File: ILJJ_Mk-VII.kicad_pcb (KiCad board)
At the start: 2 copper layers, 48.3 x 99.1 mm, 29 parts, among them J1 Conn_02x12, U1 74LS00, U10 74LS00, U11 74LS00, U2 74LS00, U3 74LS00, U4 74LS00, U5 74LS00, U6 74LS00, U7 74LS00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

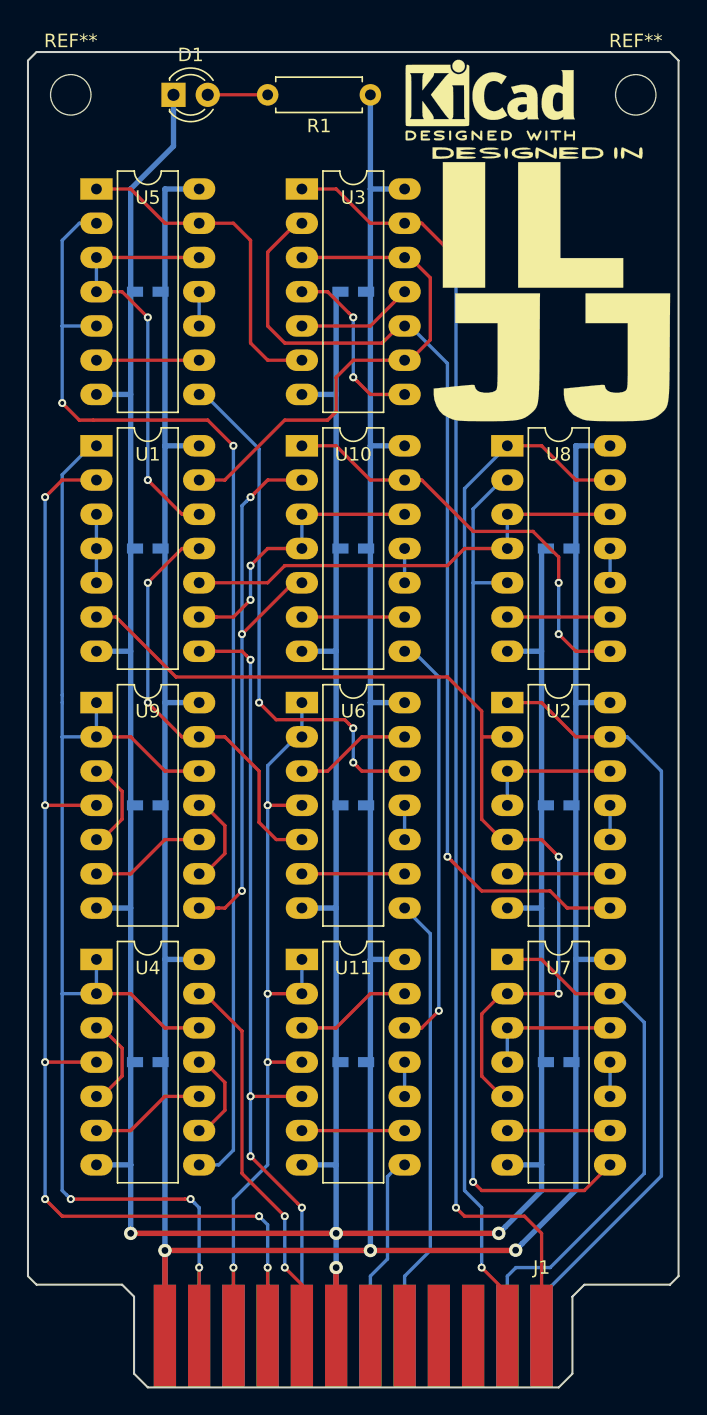
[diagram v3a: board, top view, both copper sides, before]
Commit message: [fix] ICの干渉を解消 / ILJJのロゴを小さく
かなりレイアウトが変わった
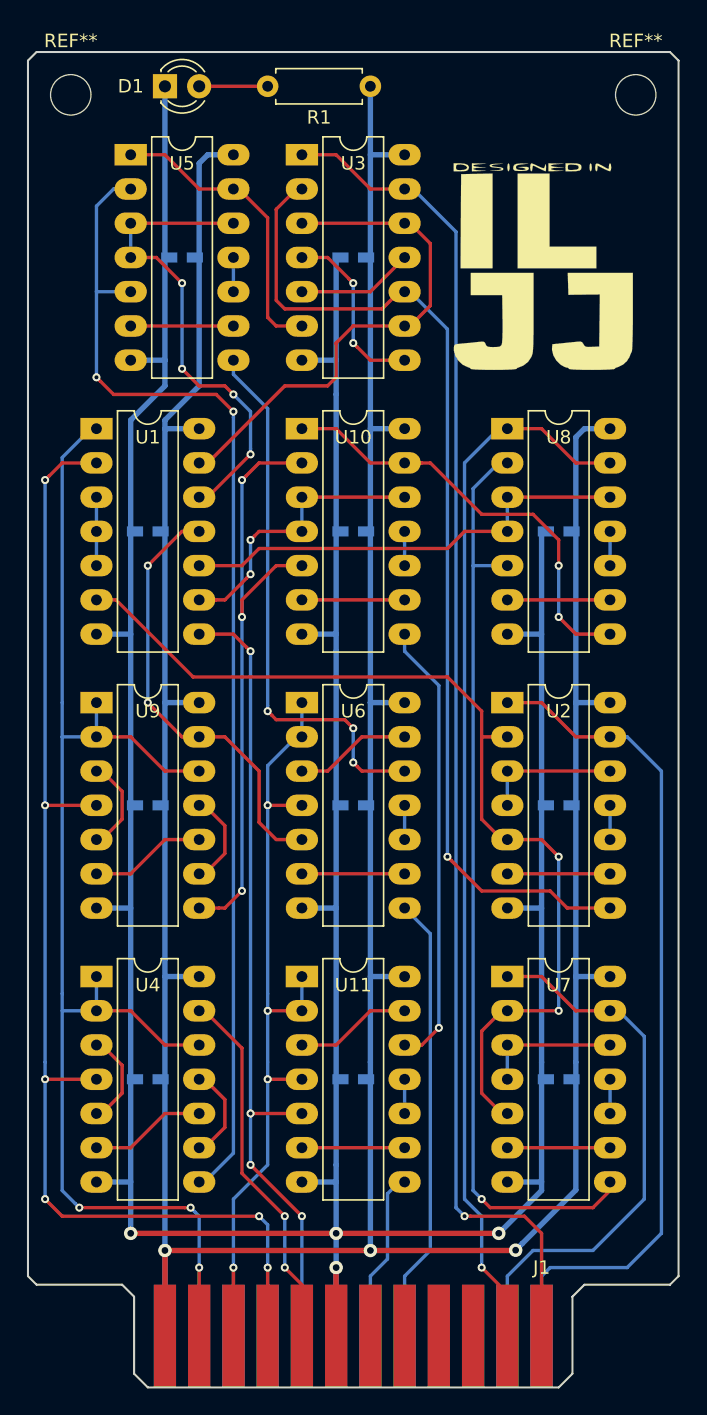
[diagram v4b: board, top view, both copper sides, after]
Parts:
- removed the G*** at (140.3, 67.9)
- removed REF***: KiCad-Logo2_6mm_SilkScreen, Symbols:KiCad-Logo2_6mm_SilkScreen
- added G***: LOGO, fplib:designed-in-ILJJ-small, F.Cu at (139.7, 66.7)
- moved C1 3.59 mm to (113.0, 66.0)
- moved U5 3.59 mm to (109.2, 58.4)
- moved U3 2.54 mm to (121.9, 58.4)
- moved C5 2.54 mm to (125.7, 66.0)
- moved U1 1.27 mm to (106.7, 78.7)
- moved U10 1.27 mm to (121.9, 78.7)
- moved U8 1.27 mm to (137.2, 78.7)
- moved C11 1.27 mm to (141.0, 127.0)
- moved C2 1.27 mm to (110.5, 86.4)
- moved C4 1.27 mm to (110.5, 127.0)
- moved C6 1.27 mm to (125.7, 86.4)
- moved C8 1.27 mm to (125.7, 127.0)
- moved C9 1.27 mm to (141.0, 86.4)
- moved U11 1.27 mm to (121.9, 119.4)
- moved U4 1.27 mm to (106.7, 119.4)
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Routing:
- net VCC: track 296.2 -> 300.9 mm
- net GND: track 278.6 -> 282.7 mm
- net Net-(U1-Pad12): track 31.7 -> 35.8 mm, vias 2 -> 4
- net /B0: track 59.1 -> 62.5 mm
- net Net-(U3-Pad6): track 25.0 -> 22.3 mm
- net /FA1_B: track 67.1 -> 69.8 mm
- net /FA1_Cin: track 43.5 -> 45.9 mm
- net /FA1_S: track 31.2 -> 33.3 mm
- net /A0: track 98.8 -> 100.9 mm, vias 2 -> 1
- net /FA0_B: track 74.7 -> 76.7 mm
- net /SUB_FLAG: track 72.3 -> 74.1 mm
- net /Cin: track 29.2 -> 27.5 mm
- net /FA0_S: track 39.3 -> 41.0 mm
- net /A1: track 77.3 -> 79.0 mm
- net Net-(U10-Pad1): track 32.5 -> 33.8 mm
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
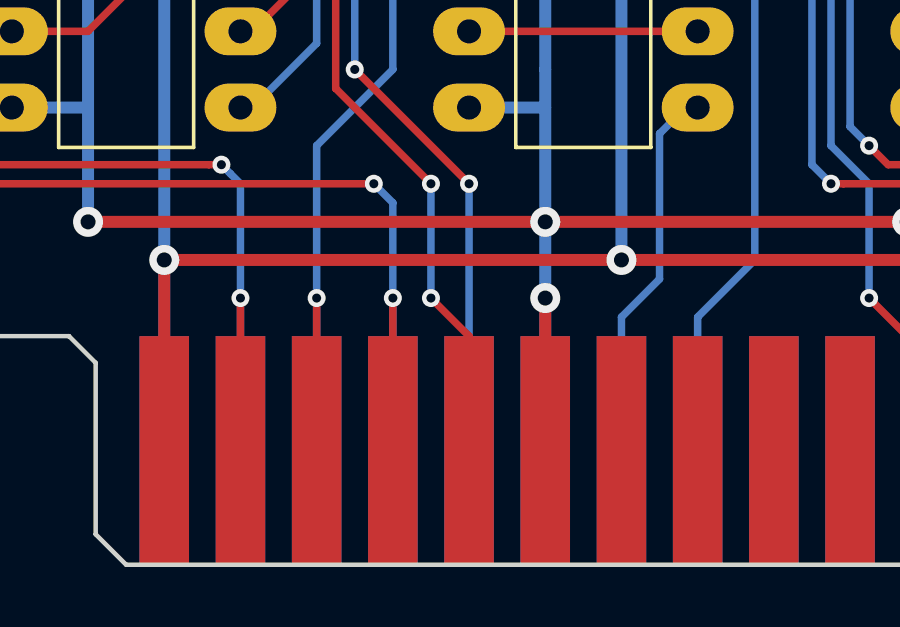
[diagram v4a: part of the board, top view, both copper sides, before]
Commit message: [change] CinとCoutを交換
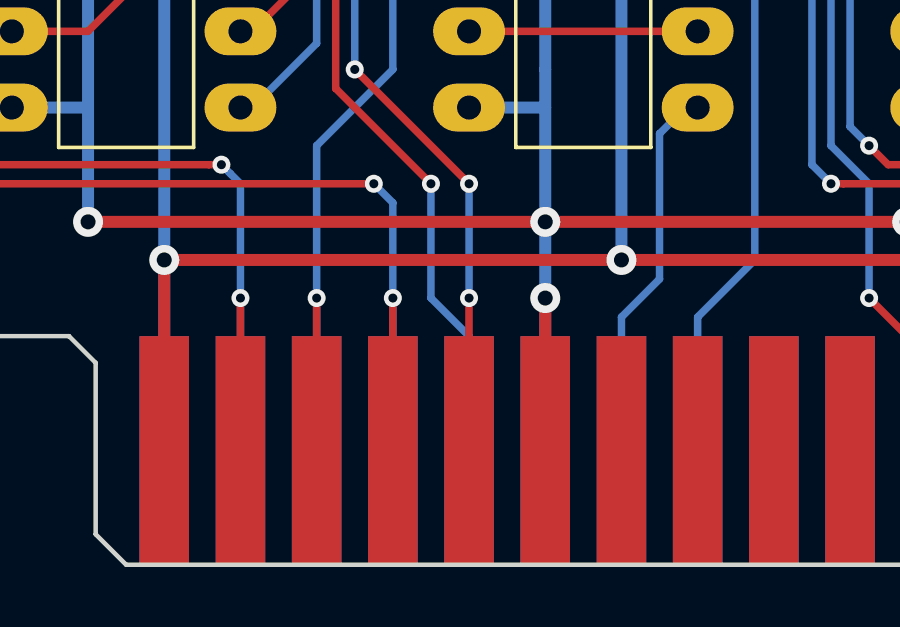
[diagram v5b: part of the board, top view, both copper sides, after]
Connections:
- J1 pad 10: /Cout -> /Cin
- J1 pad 9: /Cin -> /Cout
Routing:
- net /Cout: vias 4 -> 5
- net /Cin: vias 2 -> 1
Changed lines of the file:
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@@
       (net 6 /F0))
     (pad 9 connect rect (at -3.81 0) (size 1.651 7.62) (layers F.Cu F.Mask)
+      (net 8 /Cout))
+    (pad 10 connect rect (at -3.81 0) (size 1.651 7.62) (layers B.Cu B.Mask)
       (net 7 /Cin))
-    (pad 10 connect rect (at -3.81 0) (size 1.651 7.62) (layers B.Cu B.Mask)
-      (net 8 /Cout))
     (pad 11 connect rect (at -1.27 0) (size 1.651 7.62) (layers F.Cu F.Mask)
       (net 1 GND))
@@
   (segment (start 102.87 106.68) (end 102.87 82.55) (width 0.25) (layer B.Cu) (net 6))
   (segment (start 103.169999 82.250001) (end 102.87 82.55) (width 0.25) (layer F.Cu) (net 6))
-  (segment (start 121.92 146.05) (end 121.92 143.0655) (width 0.25) (layer F.Cu) (net 7))
-  (segment (start 121.92 142.24) (end 120.65 140.97) (width 0.25) (layer F.Cu) (net 7))
-  (via (at 120.65 140.97) (size 0.6) (drill 0.3) (layers F.Cu B.Cu) (net 7))
-  (segment (start 121.92 143.0655) (end 121.92 142.24) (width 0.25) (layer F.Cu) (net 7))
   (via (at 120.65 137.16) (size 0.6) (drill 0.3) (layers F.Cu B.Cu) (net 7))
-  (segment (start 120.65 140.97) (end 120.65 137.16) (width 0.25) (layer B.Cu) (net 7))
   (segment (start 120.65 137.16) (end 117.475 133.985) (width 0.25) (layer F.Cu) (net 7))
   (segment (start 121.92 129.54) (end 118.11 129.54) (width 0.25) (layer F.Cu) (net 8))
@@
   (segment (start 117.475 124.695) (end 114.7 121.92) (width 0.25) (layer F.Cu) (net 7))
   (segment (start 117.475 133.985) (end 117.475 124.695) (width 0.25) (layer F.Cu) (net 7))
+  (segment (start 121.92 142.24) (end 121.92 146.05) (width 0.25) (layer B.Cu) (net 7))
+  (segment (start 120.65 140.97) (end 121.92 142.24) (width 0.25) (layer B.Cu) (net 7))
+  (segment (start 120.65 137.16) (end 120.65 140.97) (width 0.25) (layer B.Cu) (net 7))
   (via (at 121.92 137.16) (size 0.6) (drill 0.3) (layers F.Cu B.Cu) (net 8))
-  (segment (start 121.92 146.05) (end 121.92 137.16) (width 0.25) (layer B.Cu) (net 8))
   (via (at 118.11 133.350004) (size 0.6) (drill 0.3) (layers F.Cu B.Cu) (net 8))
   (segment (start 118.110004 133.350004) (end 118.11 133.350004) (width 0.25) (layer F.Cu) (net 8))
@@
   (segment (start 117.810001 94.949997) (end 118.11 95.249996) (width 0.25) (layer F.Cu) (net 8))
   (segment (start 114.3 93.98) (end 116.840004 93.98) (width 0.25) (layer F.Cu) (net 8))
+  (via (at 121.92 140.97) (size 0.6) (drill 0.3) (layers F.Cu B.Cu) (net 8))
+  (segment (start 121.92 137.16) (end 121.92 140.97) (width 0.25) (layer B.Cu) (net 8))
+  (segment (start 121.92 140.97) (end 121.92 146.05) (width 0.25) (layer F.Cu) (net 8))
   (segment (start 128.27 140.335) (end 128.27 135.49) (width 0.25) (layer B.Cu) (net 10))
   (segment (start 136.525 78.74) (end 137.16 78.74) (width 0.25) (layer B.Cu) (net 17))
